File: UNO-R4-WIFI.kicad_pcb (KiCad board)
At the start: 4 copper layers, 68.6 x 53.3 mm, 266 parts, among them J1 CX90B-16P, J2 SM04B-SRSS-TB(LF)(SN), J3 PH2-06-UA, J4 SSQ-115-01-G-S, J5 19TW-746, J6 PH2-06-UA, J7 SSQ-108-01-G-S, J8 SSQ-110-01-G-S, J9 TSW-103-07-G-S, M1 ESP32-S3-MINI-1-N8, P400_SCL1 CMP-018-0004-A.4, P401_SDA1 CMP-018-0004-A.4, Q1 2N7002KT1G, Q2 2N7002KT1G, Q3 2N7002KT1G, U1 R7FA4M1AB3CFM#AA0, U2 NLASB3157DFT2G, U3 ISL854102FRZ-T, U4 TXB0108DQSR, U5 SGM2205-3.3XKC3G/TR, U6 NLASB3157DFT2G

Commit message: added drawing sheet
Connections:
- DL1 pad 1: (no net) -> Net-(DL1-K)
- DL1 pad 2: (no net) -> +5V
- DL2 pad 1: (no net) -> Net-(DL2-K)
- DL2 pad 2: (no net) -> +3V3
- DL3 pad 1: (no net) -> Net-(DL3-K)
- DL3 pad 2: (no net) -> +5V
- DL4 pad 1: (no net) -> Net-(DL4-K)
- DL4 pad 2: (no net) -> +5V
- R20 pad 1: Net-(DL2-PadC) -> Net-(DL2-K)
- R22 pad 1: Net-(DL1-PadC) -> Net-(DL1-K)
- R23 pad 1: Net-(DL2-PadC) -> Net-(DL2-K)
- R24 pad 1: Net-(DL3-PadC) -> Net-(DL3-K)
- R25 pad 1: Net-(DL4-PadC) -> Net-(DL4-K)
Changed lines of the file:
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@@
 	(net 26 "/USB_D_N")
 	(net 27 "/USB_D_P")
-	(net 28 "Net-(DL1-PadC)")
-	(net 29 "Net-(DL2-PadC)")
-	(net 30 "Net-(DL3-PadC)")
-	(net 31 "Net-(DL4-PadC)")
+	(net 28 "Net-(DL1-K)")
+	(net 29 "Net-(DL2-K)")
+	(net 30 "Net-(DL3-K)")
+	(net 31 "Net-(DL4-K)")
 	(net 32 "/ESP_DOWNLOAD")
 	(net 33 "/ESP_IO1")
@@
 			)
 		)
-		(property "Description" ""
+		(property "Description" "Light emitting diode"
 			(at 0 0 0)
 			(unlocked yes)
@@
 			)
 		)
-		(property ki_fp_filters "*LEDC1608X80N-AK*")
+		(property ki_fp_filters "LED* LED_SMD:* LED_THT:*")
 		(sheetname "Root")
 		(sheetfile "UNO-R4-WIFI.kicad_sch")
@@
 			(layers "F.Cu" "F.Paste" "F.Mask")
 			(roundrect_rratio 0.25)
+			(net 28 "Net-(DL1-K)")
+			(pinfunction "K")
+			(pintype "passive")
 		)
 		(pad "2" smd roundrect
@@
 			(layers "F.Cu" "F.Paste" "F.Mask")
 			(roundrect_rratio 0.25)
+			(net 65 "+5V")
+			(pinfunction "A")
+			(pintype "passive")
 		)
 		(model "${KICAD8_3DMODEL_DIR}/LED_SMD.3dshapes/LED_0402_1005Metric.wrl"
@@
 			)
 		)
-		(property "Description" ""
+		(property "Description" "Light emitting diode"
 			(at 0 0 0)
 			(unlocked yes)
@@
 			)
 		)
-		(property ki_fp_filters "*LEDC1608X80N-AK*")
+		(property ki_fp_filters "LED* LED_SMD:* LED_THT:*")
 		(sheetname "Root")
 		(sheetfile "UNO-R4-WIFI.kicad_sch")
@@
 			(layers "F.Cu" "F.Paste" "F.Mask")
 			(roundrect_rratio 0.25)
+			(net 29 "Net-(DL2-K)")
+			(pinfunction "K")
+			(pintype "passive")
 		)
 		(pad "2" smd roundrect
@@
 			(layers "F.Cu" "F.Paste" "F.Mask")
 			(roundrect_rratio 0.25)
+			(net 66 "+3V3")
+			(pinfunction "A")
+			(pintype "passive")
 		)
 		(model "${KICAD8_3DMODEL_DIR}/LED_SMD.3dshapes/LED_0402_1005Metric.wrl"
@@
 			)
 		)
-		(property "Description" ""
+		(property "Description" "Light emitting diode"
 			(at 0 0 -45)
 			(unlocked yes)
@@
 			)
 		)
-		(property ki_fp_filters "*LEDC1608X80N-AK*")
-		(sheetname "Root")
-		(sheetfile "UNO-R4-WIFI.kicad_sch")
 		(attr smd)
 		(fp_circle
@@
 			(layers "F.Cu" "F.Paste" "F.Mask")
 			(roundrect_rratio 0.25)
+			(net 30 "Net-(DL3-K)")
+			(pinfunction "K")
+			(pintype "passive")
 		)
 		(pad "2" smd roundrect
@@
 			(layers "F.Cu" "F.Paste" "F.Mask")
 			(roundrect_rratio 0.25)
+			(net 65 "+5V")
+			(pinfunction "A")
+			(pintype "passive")
 		)
 		(model "${KICAD8_3DMODEL_DIR}/LED_SMD.3dshapes/LED_0402_1005Metric.wrl"
@@
 			)
 		)
-		(property "Description" ""
+		(property "Description" "Light emitting diode"
 			(at 0 0 0)
 			(unlocked yes)
@@
 			)
 		)
-		(property ki_fp_filters "*LEDC1608X80N-AK*")
+		(property ki_fp_filters "LED* LED_SMD:* LED_THT:*")
 		(sheetname "Root")
 		(sheetfile "UNO-R4-WIFI.kicad_sch")
@@
 			(layers "F.Cu" "F.Paste" "F.Mask")
 			(roundrect_rratio 0.25)
+			(net 31 "Net-(DL4-K)")
+			(pinfunction "K")
+			(pintype "passive")
 		)
 		(pad "2" smd roundrect
@@
 			(layers "F.Cu" "F.Paste" "F.Mask")
 			(roundrect_rratio 0.25)
+			(net 65 "+5V")
+			(pinfunction "A")
+			(pintype "passive")
 		)
 		(model "${KICAD8_3DMODEL_DIR}/LED_SMD.3dshapes/LED_0402_1005Metric.wrl"
@@
 			(layers "F.Cu" "F.Paste" "F.Mask")
 			(roundrect_rratio 0.25)
-			(net 29 "Net-(DL2-PadC)")
+			(net 29 "Net-(DL2-K)")
 			(pintype "passive")
 		)
@@
 		(fp_arc
 			(start 3.02825 3.7125)
-			(mid 3.64887 3.83595)
+			(mid 3.648871 3.835949)
 			(end 4.175007 4.187503)
 			(stroke
@@
 			(layers "F.Cu" "F.Paste" "F.Mask")
 			(roundrect_rratio 0.25)
-			(net 28 "Net-(DL1-PadC)")
+			(net 28 "Net-(DL1-K)")
 			(pintype "passive")
 		)
@@
 			(layers "F.Cu" "F.Paste" "F.Mask")
 			(roundrect_rratio 0.25)
-			(net 31 "Net-(DL4-PadC)")
+			(net 31 "Net-(DL4-K)")
 			(pintype "passive")
 		)
@@
 			(layers "F.Cu" "F.Paste" "F.Mask")
 			(roundrect_rratio 0.25)
-			(net 29 "Net-(DL2-PadC)")
+			(net 29 "Net-(DL2-K)")
 			(pintype "passive")
 		)
@@
 			(layers "F.Cu" "F.Paste" "F.Mask")
 			(roundrect_rratio 0.25)
-			(net 30 "Net-(DL3-PadC)")
+			(net 30 "Net-(DL3-K)")
 			(pintype "passive")
 		)
@@
 		(min_thickness 0.25)
 		(filled_areas_thickness no)
-		(fill yes
+		(fill
 			(thermal_gap 0.254)
 			(thermal_bridge_width 0.254)
@@
 		(min_thickness 0.25)
 		(filled_areas_thickness no)
-		(fill yes
+		(fill
 			(thermal_gap 0.254)
 			(thermal_bridge_width 0.254)
@@
 		(min_thickness 0.25)
 		(filled_areas_thickness no)
-		(fill yes
+		(fill
 			(thermal_gap 0.254)
 			(thermal_bridge_width 0.254)
@@
 		(min_thickness 0.25)
 		(filled_areas_thickness no)
-		(fill yes
+		(fill
 			(thermal_gap 0.254)
 			(thermal_bridge_width 0.254)
@@
 		(min_thickness 0.25)
 		(filled_areas_thickness no)
-		(fill yes
+		(fill
 			(thermal_gap 0.254)
 			(thermal_bridge_width 0.254)
@@
 		(min_thickness 0.25)
 		(filled_areas_thickness no)
-		(fill yes
+		(fill
 			(thermal_gap 0.254)
 			(thermal_bridge_width 0.254)
@@
 		(min_thickness 0.25)
 		(filled_areas_thickness no)
-		(fill yes
+		(fill
 			(thermal_gap 0.254)
 			(thermal_bridge_width 0.254)
@@
 		(min_thickness 0.25)
 		(filled_areas_thickness no)
-		(fill yes
+		(fill
 			(thermal_gap 0.254)
 			(thermal_bridge_width 0.254)
@@
 		(min_thickness 0.25)
 		(filled_areas_thickness no)
-		(fill yes
+		(fill
 			(thermal_gap 0.254)
 			(thermal_bridge_width 0.254)
@@
 		(min_thickness 0.25)
 		(filled_areas_thickness no)
-		(fill yes
+		(fill
 			(thermal_gap 0.254)
 			(thermal_bridge_width 0.254)
@@
 		(min_thickness 0.25)
 		(filled_areas_thickness no)
-		(fill yes
+		(fill
 			(thermal_gap 0.254)
 			(thermal_bridge_width 0.254)

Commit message: added external schematic library
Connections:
- net /U_LEDMATRIX/ROW0 renamed /LED-MATRIX/ROW0
- net /U_LEDMATRIX/ROW1 renamed /LED-MATRIX/ROW1
- net /U_LEDMATRIX/ROW10 renamed /LED-MATRIX/ROW10
- net /U_LEDMATRIX/ROW2 renamed /LED-MATRIX/ROW2
- net /U_LEDMATRIX/ROW3 renamed /LED-MATRIX/ROW3
- net /U_LEDMATRIX/ROW4 renamed /LED-MATRIX/ROW4
- net /U_LEDMATRIX/ROW5 renamed /LED-MATRIX/ROW5
- net /U_LEDMATRIX/ROW6 renamed /LED-MATRIX/ROW6
- net /U_LEDMATRIX/ROW7 renamed /LED-MATRIX/ROW7
- net /U_LEDMATRIX/ROW8 renamed /LED-MATRIX/ROW8
- net /U_LEDMATRIX/ROW9 renamed /LED-MATRIX/ROW9

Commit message: changed power symbols
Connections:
- net +3V3 renamed +3.3V
- net +3V3_I2C renamed +3.3V_I2C
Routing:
- net +3.3V: track 95.8 -> 27.5 mm
- net (no net): track 913.2 -> 981.5 mm

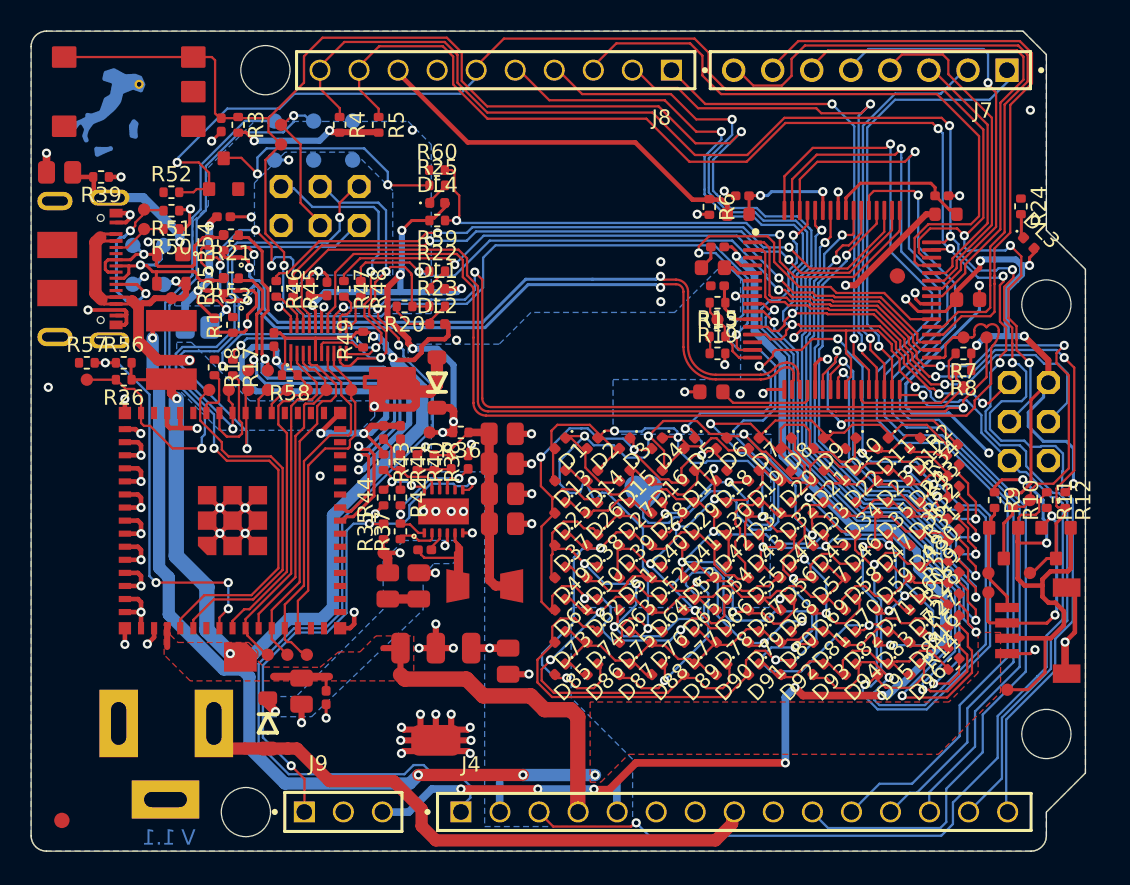
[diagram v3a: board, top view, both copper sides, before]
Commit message: updated capacitors symbols + footprints
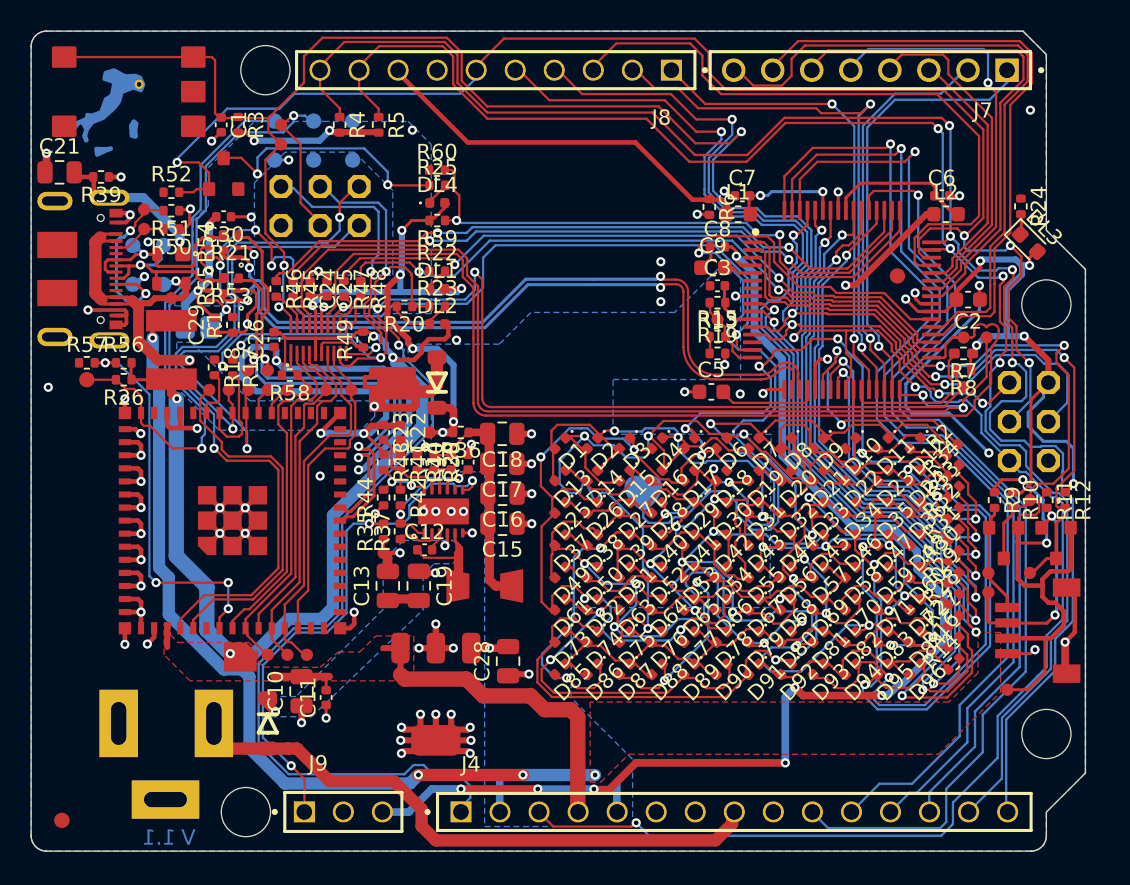
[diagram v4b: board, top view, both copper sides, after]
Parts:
- 3V3_IC1, 3V3_TOP1, 5V_TOP1, BUCK_IN_TOP1, CC1, CC2, D+_TOP1, D-_TOP1, ESP_DOWNLOAD_TOP1, ESP_IO1, ESP_IO4, ESP_IO5, ESP_IO6, ESP_IO7, ESP_IO8, ESP_IO9, ESP_MTCK1, ESP_MTDI1, ESP_MTDO1, ESP_MTMS1, EXT_SCL1, EXT_SDA1, MD1, P400_SCL1, P401_SDA1, RES1, SWCLK1, SWDIO1, VCONN_TOP1, VIN_TOP1, uC_VBUS1: footprint footprints:TP-0.8MM -> external_footprints:TP-0.8MM
- C1, C11, C12, C14, C20, C22, C23, C24, C25, C26, C29, C3, C30, C6, C7, C8: footprint Vault:CAP-0402 -> Capacitor_SMD:C_0402_1005Metric
- C10, C13, C15, C16, C17, C18, C19, C21, C28: footprint Vault:CAP-0805 -> Capacitor_SMD:C_0805_2012Metric
- C2, C5, C9: footprint Vault:CAP-0603 -> Capacitor_SMD:C_0603_1608Metric
- D+1, D-1, ESP_DOWNLOAD_BOTTOM1, ESP_EN_BOTTOM1, GND1, GND2, LOVE1, VBUS_CONN1: footprint footprints:TP-1.00MM -> external_footprints:TP-1.00MM
- DL3: footprint LED_SMD:LED_0402_1005Metric -> LED_SMD:LED_0603_1608Metric
- ESP_EN_TOP1: footprint footprints:TP-0.8MM -> external_footprints:TP-1.00MM
- L1, L2: footprint Vault:L-0603 -> Inductor_SMD:L_0603_1608Metric
- R7: footprint Resistor_SMD:R_0402_1005Metric -> Resistor_SMD:R_0402_1005Metric_Pad0.72x0.64mm_HandSolder
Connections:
- C10 pad 1: GND -> +3.3V
- C10 pad 2: +3.3V -> GND
- C11 pad 1: GND -> +3.3V
- C11 pad 2: +3.3V -> GND
- C12 pad 1: Net-(U3-PHASE) -> Net-(U3-BOOT)
- C12 pad 2: Net-(U3-BOOT) -> Net-(U3-PHASE)
- C13 pad 1: Net-(C13-Pad1) -> Net-(U3-VIN)
- C13 pad 2: Net-(U3-VIN) -> Net-(C13-Pad2)
- C14 pad 1: Net-(U3-FB) -> Net-(C14-Pad1)
- C14 pad 2: Net-(C14-Pad2) -> Net-(U3-FB)
- C15 pad 1: GND -> Net-(C14-Pad1)
- C15 pad 2: Net-(C14-Pad2) -> GND
- C16 pad 1: GND -> Net-(C14-Pad1)
- C16 pad 2: Net-(C14-Pad2) -> GND
- C17 pad 1: GND -> Net-(C14-Pad1)
- C17 pad 2: Net-(C14-Pad2) -> GND
- C18 pad 1: GND -> Net-(C14-Pad1)
- C18 pad 2: Net-(C14-Pad2) -> GND
- C19 pad 1: GND -> Net-(C13-Pad2)
- C19 pad 2: Net-(C13-Pad1) -> GND
- C21 pad 1: GND -> /SHIELD1
- C21 pad 2: /SHIELD1 -> GND
- C22 pad 1: GND -> Net-(C22-Pad1)
- C22 pad 2: Net-(C22-Pad2) -> GND
- C23 pad 1: GND -> Net-(U3-COMP)
- C23 pad 2: Net-(U3-COMP) -> GND
- C24 pad 1: GND -> +5V
- C24 pad 2: +5V -> GND
- C25 pad 1: GND -> +5V
- C25 pad 2: +5V -> GND
- C26 pad 1: GND -> +3.3V
- C26 pad 2: +3.3V -> GND
- C28 pad 1: GND -> +5V
- C28 pad 2: +5V -> GND
- C29 pad 1: GND -> +5V
- C29 pad 2: +5V -> GND
- C30 pad 1: GND -> +5V
- C30 pad 2: +5V -> GND
- C7 pad 1: GND -> /VREFH0
- C7 pad 2: /VREFH0 -> GND
- C8 pad 1: GND -> /VBATT
- C8 pad 2: /VBATT -> GND
- C9 pad 1: GND -> Net-(U1-VCL)
- C9 pad 2: Net-(U1-VCL) -> unconnected-(C9-Pad2)
- L3 pad 2: Net-(C14-Pad2) -> Net-(C14-Pad1)
- R36 pad 1: Net-(C14-Pad2) -> Net-(C14-Pad1)
- R38 pad 1: Net-(C14-Pad2) -> Net-(C14-Pad1)
- R41 pad 2: Net-(C22-Pad2) -> Net-(C22-Pad1)
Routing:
- net (no net): track 981.5 -> 1000.0 mm
- net Net-(C14-Pad2): track 15.4 -> 0.00 mm
- net GND: track 189.6 -> 179.5 mm, vias 81 -> 69
- net +5V: track 126.0 -> 131.0 mm, vias 22 -> 25
- net Net-(C14-Pad1): track 0.00 -> 4.22 mm, vias 0 -> 4
- net +3.3V: track 27.5 -> 25.0 mm, vias 4 -> 6
- net Net-(C13-Pad1): track 2.02 -> 0.00 mm
- net /SHIELD1: track 10.9 -> 12.2 mm, vias 2 -> 3
- net Net-(C13-Pad2): track 0.00 -> 1.09 mm, vias 0 -> 1
- net Net-(C22-Pad2): track 1.03 -> 0.00 mm
- net /VREFH0: track 7.33 -> 8.21 mm, vias 2 -> 3
